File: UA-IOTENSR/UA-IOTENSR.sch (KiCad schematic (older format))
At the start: 4 parts, among them SW1 SW_DPST, U1 ESP32-S3-MINI-1, U102 SCD4X

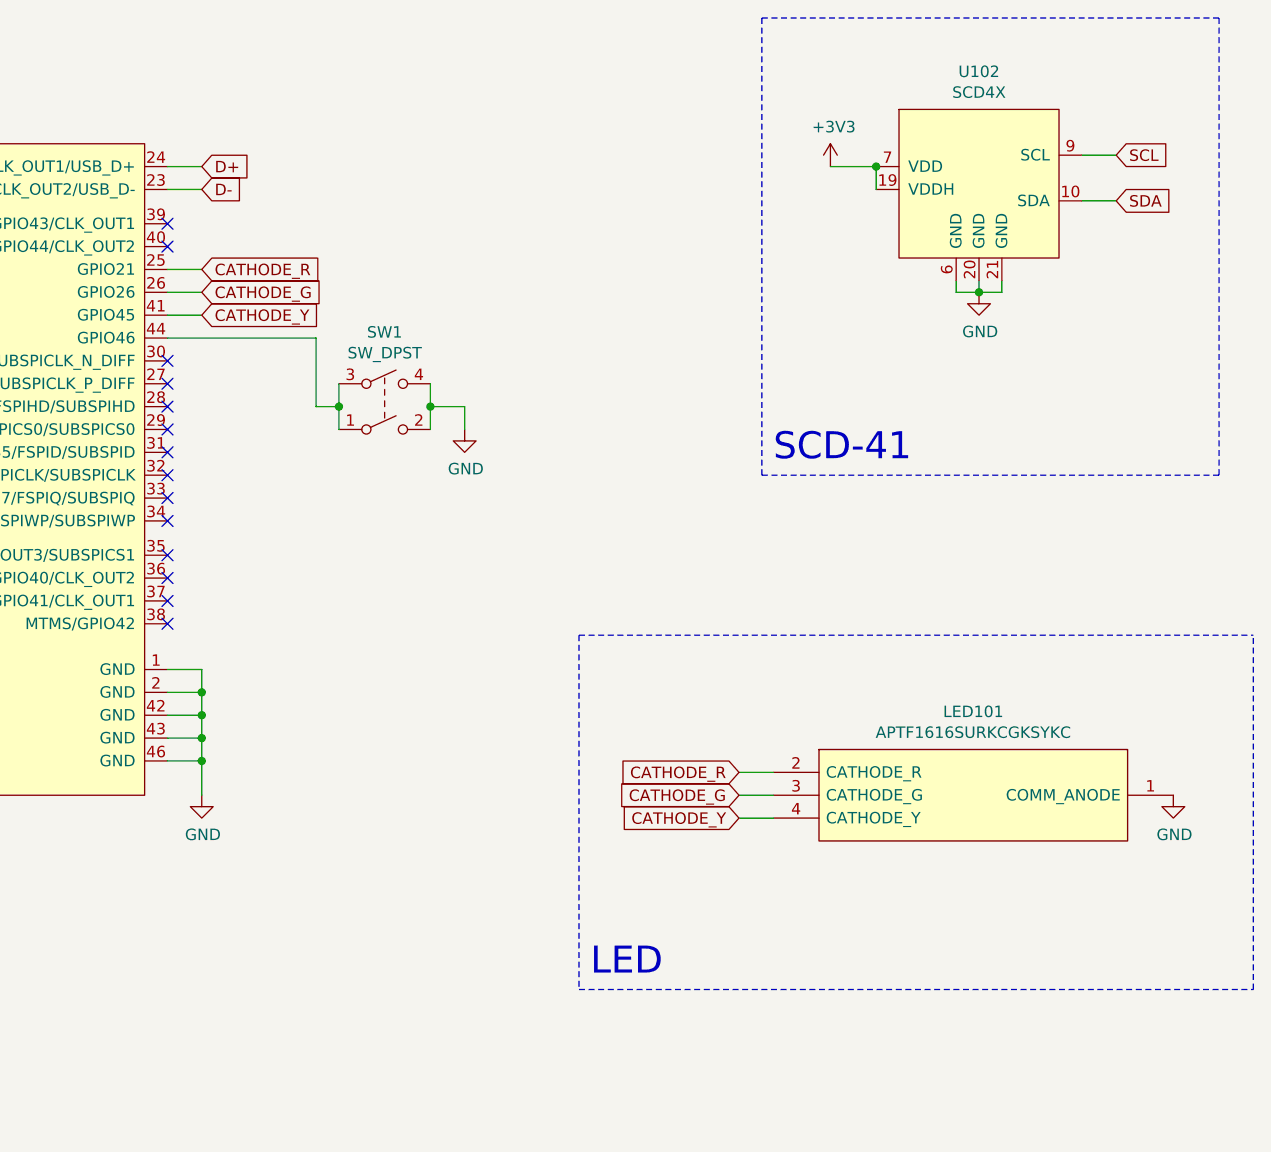
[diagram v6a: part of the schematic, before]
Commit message: Assigned footprints to all symbols, removed unused parts
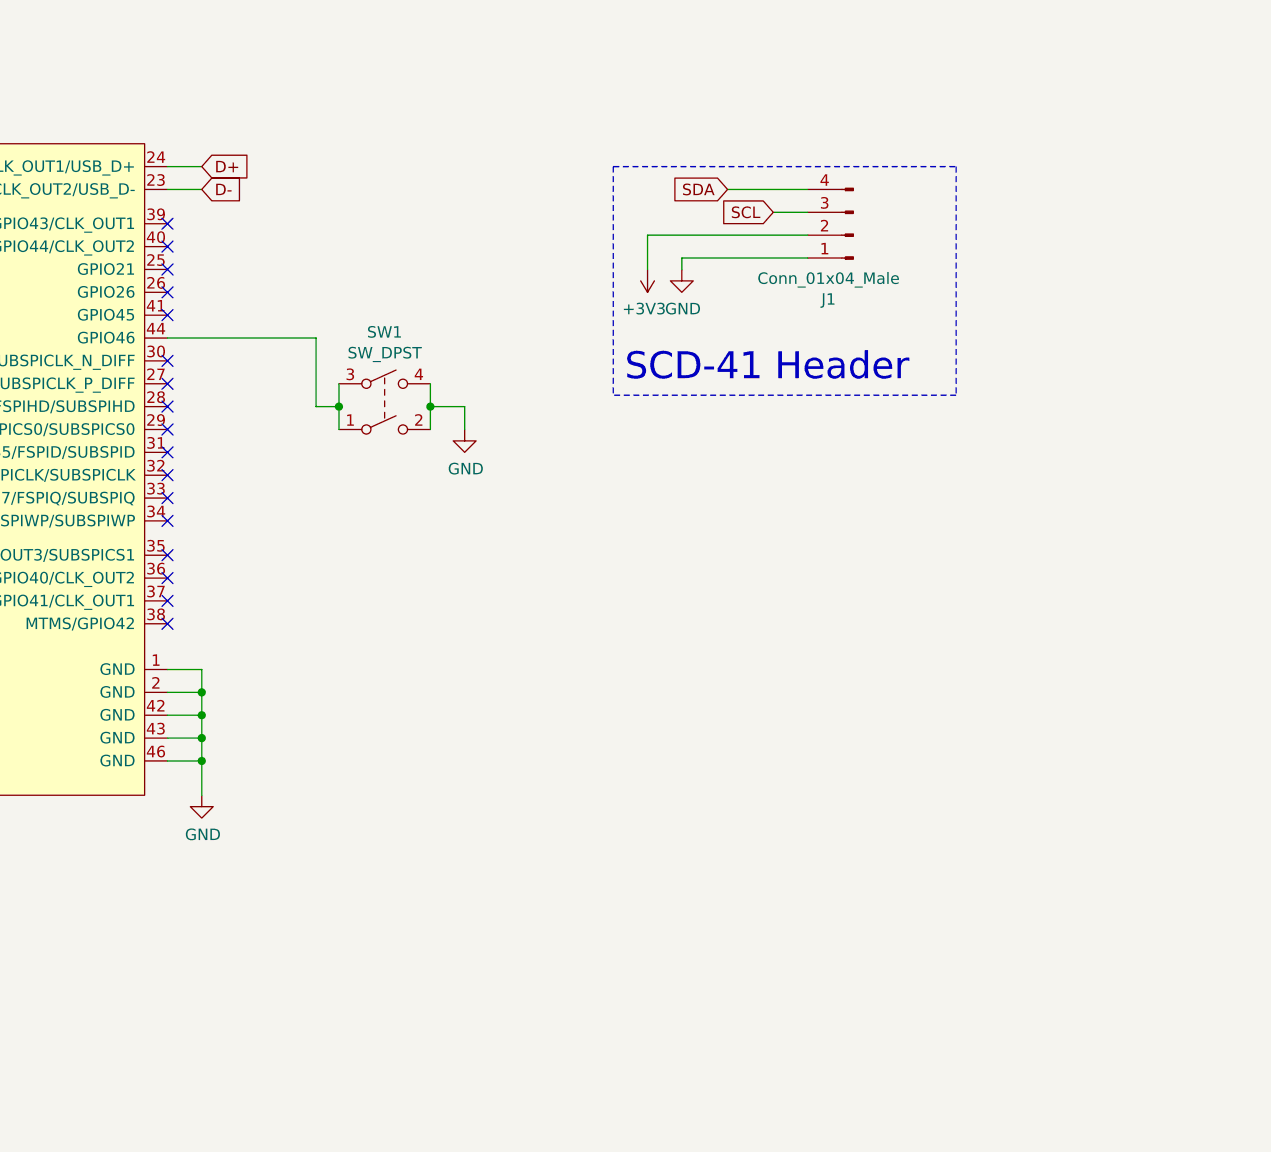
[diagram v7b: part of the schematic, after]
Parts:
- removed LED101: APTF1616SURKCGKSYKC, SamacSys_Parts:KPTF1616RGBC11, symbol UA-IOTENSR-rescue:APTF1616SURKCGKSYKC-Samacs
- removed U102: SCD4X, Connector_PinSocket_2.54mm:PinSocket_1x04_P2.54mm_Vertical, symbol SCD4X:SCD4X
- added J1: Conn_01x04_Male, Connector_PinSocket_2.54mm:PinSocket_1x04_P2.54mm_Vertical, symbol Connector:Conn_01x04_Male
- U1: footprint Espressif:ESP32-S3-MINI-1 -> ESP32-S3-MINI-1-N8:XCVR_ESP32-S3-MINI-1-N8
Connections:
- net labels removed: CATHODE_G, CATHODE_R, CATHODE_Y
- wire segments 44 -> 35
- no-connect marks 31 -> 34
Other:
- note added: "SCD-41 Header"
- note removed: "LED"
- note removed: "SCD-41"
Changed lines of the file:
@@
 Text Notes 7000 7000 0    236  ~ 0
 ESP32 Schematic
-$Comp
-L SCD4X:SCD4X U102
-U 1 1 61B02C43
-P 9900 1450
-AR Path="/61B02C43" Ref="U102"  Part="1"
-AR Path="/61A1DC3C/61B02C43" Ref="U?"  Part="1"
-F 0 "U102" H 9900 1915 50  0000 C CNN
-F 1 "SCD4X" H 9900 1824 50  0000 C CNN
-F 2 "Connector_PinSocket_2.54mm:PinSocket_1x04_P2.54mm_Vertical" H 9900 1900 50  0001 C CNN
-F 3 "" H 9900 1900 50  0001 C CNN
-	1    9900 1450
-	1    0    0    -1
-$EndComp
-Wire Wire Line
-	10350 1350 10500 1350
-Wire Wire Line
-	10350 1550 10500 1550
-Text GLabel 10500 1350 2    50   Input ~ 0
+Wire Wire Line
+	9150 1600 9000 1600
+Text GLabel 9000 1600 0    50   Input ~ 0
 SCL
-Text GLabel 10500 1550 2    50   Input ~ 0
+Text GLabel 8800 1500 0    50   Input ~ 0
 SDA
-Wire Wire Line
-	9800 1900 9800 1950
-Wire Wire Line
-	9800 1950 9900 1950
-Wire Wire Line
-	10000 1950 10000 1900
-Wire Wire Line
-	9900 1900 9900 1950
-Connection ~ 9900 1950
-Wire Wire Line
-	9900 1950 10000 1950
-$Comp
-L power:GND #PWR0105
-U 1 1 61B02C53
-P 9900 1950
-AR Path="/61B02C53" Ref="#PWR0105"  Part="1"
-AR Path="/61A1DC3C/61B02C53" Ref="#PWR?"  Part="1"
-F 0 "#PWR0105" H 9900 1700 50  0001 C CNN
-F 1 "GND" H 9905 1777 50  0000 C CNN
-F 2 "" H 9900 1950 50  0001 C CNN
-F 3 "" H 9900 1950 50  0001 C CNN
-	1    9900 1950
-	1    0    0    -1
-$EndComp
-Wire Wire Line
-	9450 1400 9250 1400
-Wire Wire Line
-	9450 1500 9450 1400
-Connection ~ 9450 1400
 $Comp
 L power:+3V3 #PWR0104
 U 1 1 61B02C5C
-P 9250 1400
-F 0 "#PWR0104" H 9250 1250 50  0001 C CNN
-F 1 "+3V3" H 9265 1573 50  0000 C CNN
-F 2 "" H 9250 1400 50  0001 C CNN
-F 3 "" H 9250 1400 50  0001 C CNN
-	1    9250 1400
-	1    0    0    -1
-$EndComp
-Wire Notes Line
-	8950 750  10950 750
-Wire Notes Line
-	10950 2750 8950 2750
-Text Notes 9000 2700 0    118  ~ 0
-SCD-41
-$Comp
-L UA-IOTENSR-rescue:APTF1616SURKCGKSYKC-Samacs LED101
-U 1 1 61AF43CE
-P 9200 4050
-F 0 "LED101" H 9875 4315 50  0000 C CNN
-F 1 "APTF1616SURKCGKSYKC" H 9875 4224 50  0000 C CNN
-F 2 "SamacSys_Parts:KPTF1616RGBC11" H 10950 4150 50  0001 L CNN
-F 3 "" H 9150 3850 50  0001 L CNN
-F 4 "Standard LEDs - SMD RGY 1616 SMD" H 11150 3850 50  0001 L CNN "Description"
-F 5 "0.9" H 11150 3750 50  0001 L CNN "Height"
-F 6 "604-APTF1616KCGKSYKC" H 11150 3650 50  0001 L CNN "Mouser Part Number"
-F 7 "https://www.mouser.co.uk/ProductDetail/Kingbright/APTF1616SURKCGKSYKC?qs=FESYatJ8odK7UleJtP4p0g%3D%3D" H 11350 3550 50  0001 L CNN "Mouser Price/Stock"
-F 8 "Kingbright" H 11350 3450 50  0001 L CNN "Manufacturer_Name"
-F 9 "APTF1616SURKCGKSYKC" H 11350 3350 50  0001 L CNN "Manufacturer_Part_Number"
-	1    9200 4050
-	1    0    0    -1
-$EndComp
-Text Notes 8200 4950 0    118  ~ 0
-LED
-Wire Notes Line
-	8950 2750 8950 750
-Wire Notes Line
-	10950 750  10950 2750
-Wire Notes Line
-	11100 5000 11100 3450
-Wire Notes Line
-	8150 3450 8150 5000
-Wire Wire Line
-	6350 1950 6500 1950
-Text GLabel 6500 1950 2    50   Input ~ 0
-CATHODE_G
-Text GLabel 6500 1850 2    50   Input ~ 0
-CATHODE_R
-Wire Wire Line
-	6350 1850 6500 1850
-Wire Wire Line
-	6350 2050 6500 2050
-Text GLabel 6500 2050 2    50   Input ~ 0
-CATHODE_Y
-Wire Wire Line
-	9000 4150 8850 4150
-Text GLabel 8850 4150 0    50   Input ~ 0
-CATHODE_G
-Text GLabel 8850 4050 0    50   Input ~ 0
-CATHODE_R
-Wire Wire Line
-	9000 4050 8850 4050
-Wire Wire Line
-	9000 4250 8850 4250
-Text GLabel 8850 4250 0    50   Input ~ 0
-CATHODE_Y
-$Comp
-L power:GND #PWR0106
-U 1 1 61AFFCA4
-P 10750 4150
-F 0 "#PWR0106" H 10750 3900 50  0001 C CNN
-F 1 "GND" H 10755 3977 50  0000 C CNN
-F 2 "" H 10750 4150 50  0001 C CNN
-F 3 "" H 10750 4150 50  0001 C CNN
-	1    10750 4150
-	1    0    0    -1
-$EndComp
-Wire Notes Line
-	8150 3450 11100 3450
-Wire Notes Line
-	8150 5000 11100 5000
+P 8450 1850
+F 0 "#PWR0104" H 8450 1700 50  0001 C CNN
+F 1 "+3V3" H 8465 2023 50  0000 C CNN
+F 2 "" H 8450 1850 50  0001 C CNN
+F 3 "" H 8450 1850 50  0001 C CNN
+	1    8450 1850
+	-1   0    0    1
+$EndComp
+Text Notes 8350 2350 0    118  ~ 0
+SCD-41 Header
 Wire Wire Line
 	7000 2450 7100 2450
@@
 F 0 "U1" H 4025 4165 50  0000 C CNN
 F 1 "ESP32-S3-MINI-1" H 4025 4074 50  0000 C CNN
-F 2 "Espressif:ESP32-S3-MINI-1" H 4050 1000 50  0001 C CNN
+F 2 "ESP32-S3-MINI-1-N8:XCVR_ESP32-S3-MINI-1-N8" H 4050 1000 50  0001 C CNN
 F 3 "" H 4050 2950 50  0001 C CNN
 	1    4050 2650
@@
 NoConn ~ 6350 1750
 NoConn ~ 6350 1650
+NoConn ~ 6350 2050
+NoConn ~ 6350 1950
+NoConn ~ 6350 1850
+$Comp
+L Connector:Conn_01x04_Male J1
+U 1 1 6209986D
+P 9350 1700
+F 0 "J1" H 9458 1981 50  0000 C CNN
+F 1 "Conn_01x04_Male" H 9458 1890 50  0000 C CNN
+F 2 "Connector_PinSocket_2.54mm:PinSocket_1x04_P2.54mm_Vertical" H 9350 1700 50  0001 C CNN
+F 3 "~" H 9350 1700 50  0001 C CNN
+	1    9350 1700
+	-1   0    0    1
+$EndComp
+$Comp
+L power:GND #PWR0105
+U 1 1 620A1AD1
+P 8600 1850
+F 0 "#PWR0105" H 8600 1600 50  0001 C CNN
+F 1 "GND" H 8605 1677 50  0000 C CNN
+F 2 "" H 8600 1850 50  0001 C CNN
+F 3 "" H 8600 1850 50  0001 C CNN
+	1    8600 1850
+	1    0    0    -1
+$EndComp
+Wire Wire Line
+	8600 1800 8600 1850
+Wire Wire Line
+	8600 1800 9150 1800
+Wire Wire Line
+	8450 1850 8450 1700
+Wire Wire Line
+	8450 1700 9150 1700
+Wire Wire Line
+	8800 1500 9150 1500
+Wire Notes Line
+	8300 1400 9800 1400
+Wire Notes Line
+	9800 1400 9800 2400
+Wire Notes Line
+	9800 2400 8300 2400
+Wire Notes Line
+	8300 1400 8300 2400
 $EndSCHEMATC

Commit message: Completed regulator circuit; switched to 4-layer board setup
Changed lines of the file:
@@
 Wire Wire Line
 	9150 1600 9000 1600
+Text GLabel 8800 1500 0    50   Input ~ 0
+SCL
 Text GLabel 9000 1600 0    50   Input ~ 0
-SCL
-Text GLabel 8800 1500 0    50   Input ~ 0
 SDA
 $Comp
